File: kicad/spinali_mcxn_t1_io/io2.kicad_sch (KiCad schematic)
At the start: 32 parts, among them J11 ESC1, J12 ESC2, J13 RTC_BAT, J8 GPS, Q1 NX138BKMYL, SW1 CHS-01TA

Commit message: Finished IO board layout positioning. Started routing.
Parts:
- J8: footprint Connector_JST:JST_GH_SM10B-GHS-TB_1x10-1MP_P1.25mm_Horizontal -> Connector_JST:JST_GH_BM10B-GHS-TBT_1x10-1MP_P1.25mm_Vertical
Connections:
- net at D18.2 (IO_2): now also D18.9 (NC_3)
- net at D16.2 (IO_2): now also D16.9 (NC_3)
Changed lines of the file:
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@@
 			)
 		)
-		(property "Footprint" "Connector_JST:JST_GH_SM10B-GHS-TB_1x10-1MP_P1.25mm_Horizontal"
+		(property "Footprint" "Connector_JST:JST_GH_BM10B-GHS-TBT_1x10-1MP_P1.25mm_Vertical"
 			(at 224.79 84.074 0)
 			(effects

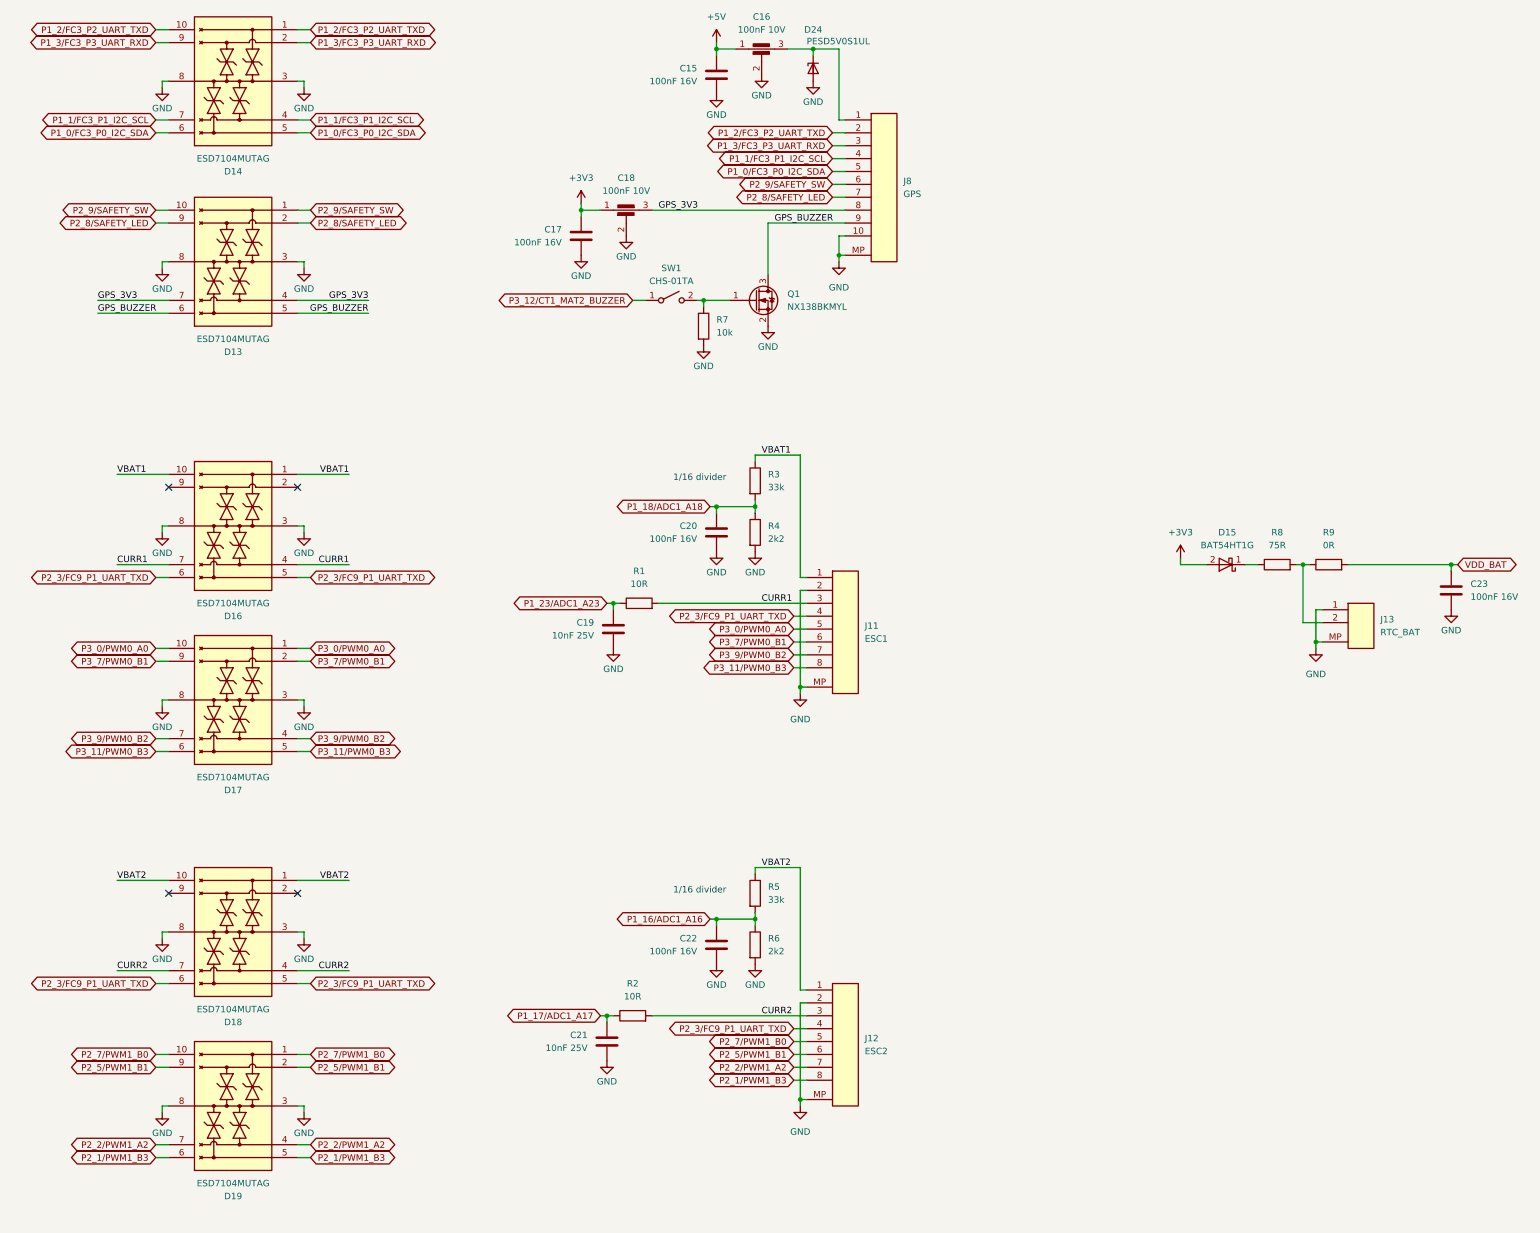
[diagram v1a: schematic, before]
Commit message: Updated schematic and layout after review (ready for production)
- Replaced TVS diode at ESC1 and ESC2 connector with higher voltage one.
- Replaced MUTAG7104 TVS with single TVS at some places to reduce cost.
- Added 1k5 pull-down resistor on GPS safety switch.
- Generated all production files.
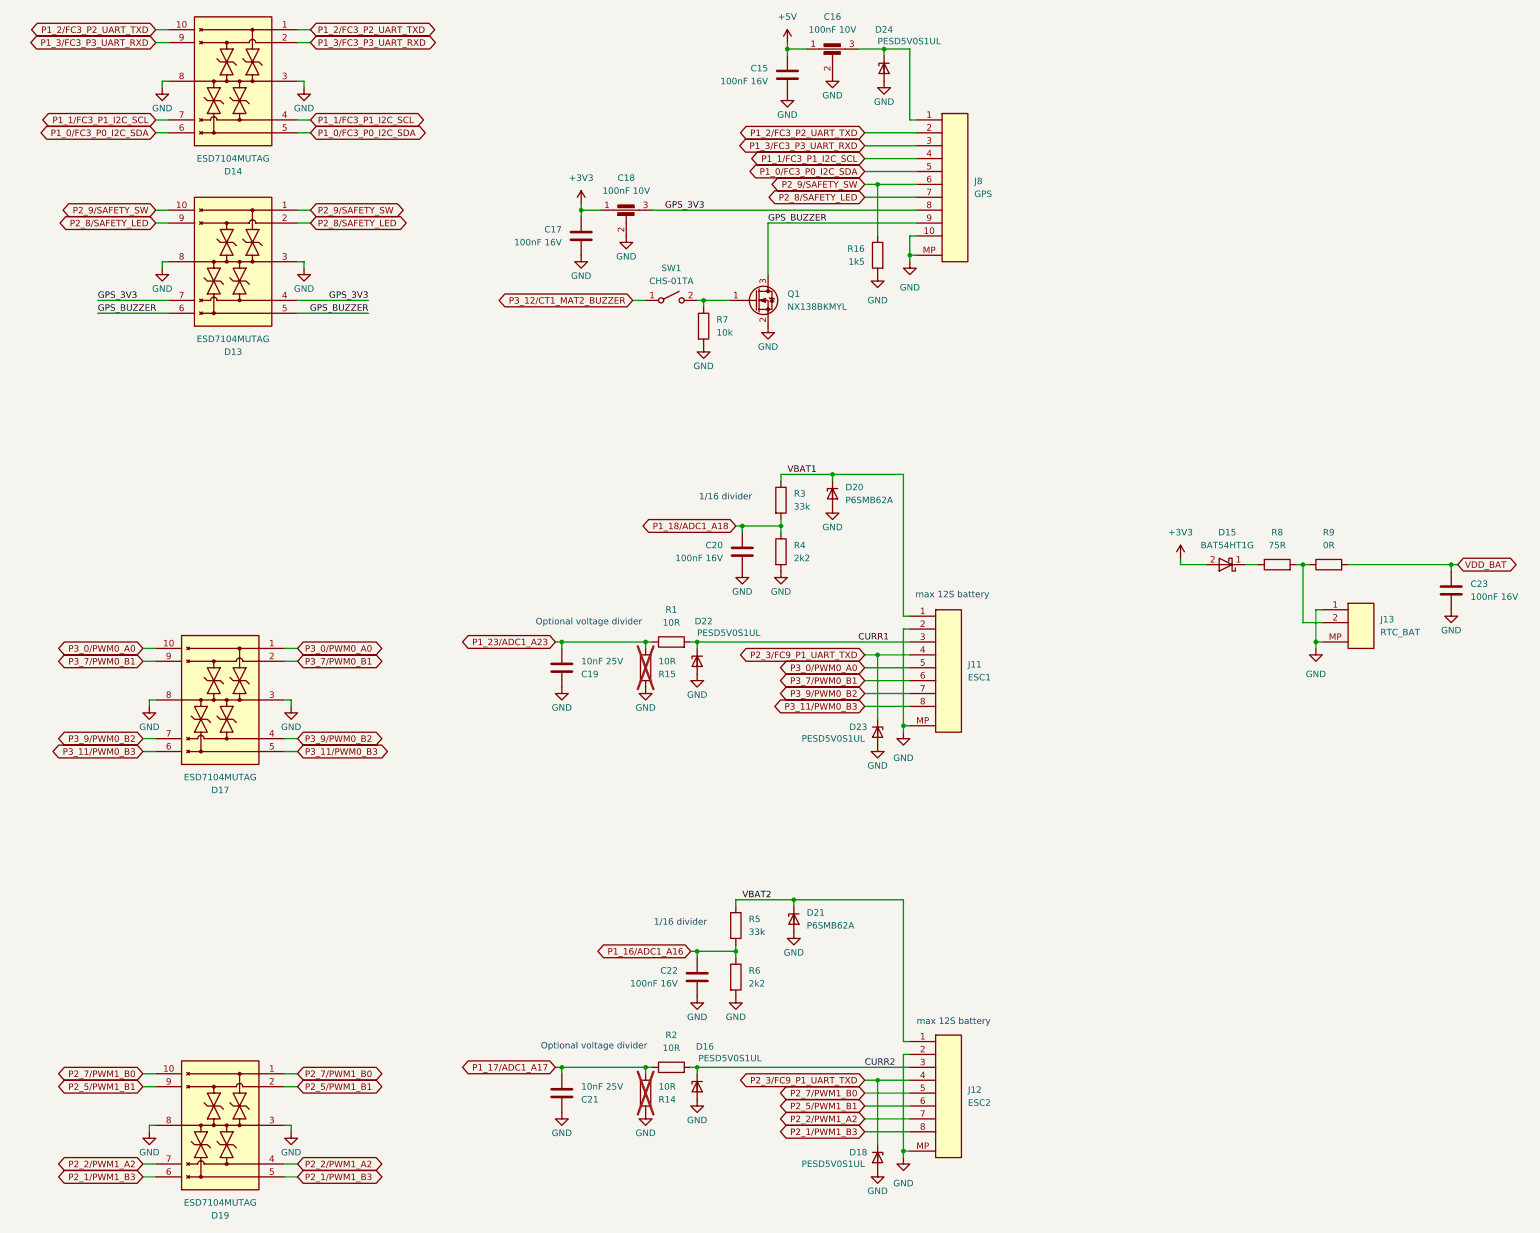
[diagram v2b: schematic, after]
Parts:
- removed D16, D18: ESD7104MUTAG, TVS:ESD8104MUTAG, symbol TVS:ESD7104MUTAG
- added D16, D18, D22, D23: PESD5V0S1UL, TVS:PESD5V0S1ULD315, symbol TVS:PESD5V0S1UL
- added D20, D21: P6SMB62A, TVS:SOD1002-1, symbol TVS:P6SMB62A
- added R14, R15: 10R, Resistor_SMD:R_0402_1005Metric, symbol Device:R
- added R16: 1k5, Resistor_SMD:R_0402_1005Metric, symbol Device:R
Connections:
- net CURR1: now also D22.1 (K1)
- net CURR2: now also D16.1 (K1)
- net GND: now also C19.1, C21.1, D16.2 (A), D18.2 (A), D20.2 (A), D21.2 (A), D22.2 (A), D23.2 (A), R14.2, R15.2, R16.2; no longer C19.2, C21.2
- net P1_17/ADC1_A17: now also C21.2, R14.1; no longer C21.1
- net P1_23/ADC1_A23: now also C19.2, R15.1; no longer C19.1
- net P2_3/FC9_P1_UART_TXD: now also D18.1 (K1), D23.1 (K1)
- net P2_9/SAFETY_SW: now also R16.1
- net VBAT1: now also D20.1 (K1)
- net VBAT2: now also D21.1 (K1)
- no-connect marks 4 -> 0
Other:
- note added: "Optional voltage divider"
- note added: "max 12S battery"
- moved on the sheet: C15, C16, C19, C20, C21, C22, D17, D19, D24, J11, J12, J8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

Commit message: Updated MCXN-T1 IO board
- Fixed that JST GH connectors are now the correct part number.
- Updated silkscreen positioning.
- Generated production files for Eurocircuits (global) and JLCPCB
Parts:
- J8: DigiKey 455-SM10B-GHS-TBCT-ND -> 455-BM10B-GHS-TBTCT-ND; MFPN SM10B-GHS-TB -> BM10B-GHS-TBT
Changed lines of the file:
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@@
 			)
 		)
-		(property "MFPN" "SM10B-GHS-TB"
+		(property "MFPN" "BM10B-GHS-TBT"
 			(at 238.76 88.646 0)
 			(effects
@@
 			)
 		)
-		(property "DigiKey" "455-SM10B-GHS-TBCT-ND"
+		(property "DigiKey" "455-BM10B-GHS-TBTCT-ND"
 			(at 238.76 90.932 0)
 			(effects
